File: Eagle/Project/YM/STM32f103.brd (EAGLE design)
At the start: 160 x 100 mm, 76 parts, among them IC1 YM3812, IC10 YM3812, IC11 YM3014B, IC12 LM358N, IC13 BA033CC0T, IC14 74ALS04N, IC15 6N136, IC2 YM3014B, IC3 LM358N, IC4 YM3812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

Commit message: LCD BOOTLOADER HEADER
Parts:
- added SV1: (no value), con-amp-mt:S06P
- added X3: (no value), con-weidmueller-sl35:90F-4
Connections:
- new net LCD-SPI-CS: SV1.4, U1.16
- net 3.3V: now also X3.1
- net 5V: now also SV1.5
- net EXP-SPI-CLK: now also SV1.1
- net EXP-SPI-MISO: now also SV1.2
- net EXP-SPI-MOSI: now also SV1.3
- net GND: now also SV1.6, X3.4
- net IO7: no longer U1.16
- net SW-CLK: now also X3.3
- net SW-DIO: now also X3.2
- net USART-TX-M4: now also X2.4
- net YM1-CS: no longer U1.51
- net YM2-CS: now also U1.51

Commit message: Eerste versie PCB - Nog niet gerout/gerouted/geroutedt. Ter review voor plaatsing componenten.
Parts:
- moved SL1 274.0 mm to (144.8, 68.6), turned to 270 degrees
- moved SL2 264.9 mm to (144.8, 36.8), turned to 270 degrees
- moved C38 259.5 mm to (144.8, 16.5)
- moved R6 256.8 mm to (148.6, 16.5)
- moved X3 251.1 mm to (63.5, 95.2), turned to 180 degrees
- moved CRYSTAL2 250.6 mm to (144.8, 20.3)
- moved C39 246.7 mm to (151.1, 2.54)
- moved R7 245.6 mm to (141.0, 16.5), turned to 180 degrees
- moved IC14 244.3 mm to (143.5, 8.89), turned to 180 degrees
- moved C30 244.2 mm to (132.1, 11.4)
- moved IC6 235.2 mm to (127.0, 66.0), turned to 180 degrees
- moved C29 230.6 mm to (120.7, 11.4)
- moved C28 229.1 mm to (120.7, 7.62)
- moved IC3 223.5 mm to (127.0, 90.2), turned to 180 degrees
- moved IC11 221.8 mm to (115.6, 17.8), turned to 180 degrees
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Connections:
- removed net N$28: C39.2
- net 5V: now also C39.2
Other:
- board size 160 x 100 mm -> 156.2 x 102.5 mm

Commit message: Eerste versie PCB
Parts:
- moved X2 66.1 mm to (26.7, 27.9), turned to 180 degrees
- moved J7 43.8 mm to (49.5, 17.8)
- moved J3 43.4 mm to (49.5, 6.35)
- moved SL2 43.2 mm to (144.8, 80.0)
- moved X3 24.7 mm to (39.4, 90.2)
- moved SV1 21.1 mm to (61.0, 11.4), turned to 90 degrees
- moved SL1 19.0 mm to (144.8, 49.5)
- moved J10 18.9 mm to (35.6, 17.8)
- moved J8 18.9 mm to (7.62, 17.8)
- moved J9 18.9 mm to (21.6, 17.8)
- moved J4 18.1 mm to (7.62, 6.35)
- moved J5 18.1 mm to (21.6, 6.35)
- moved J6 18.1 mm to (35.6, 6.35)
- moved C6 11.5 mm to (64.8, 66.0)
- moved C7 8.13 mm to (48.3, 74.9)
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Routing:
- net GND: track 0.00 -> 954.3 mm, vias 0 -> 45
- net 5V: track 0.00 -> 613.1 mm, vias 0 -> 24
- net 3.3V: track 0.00 -> 416.1 mm, vias 0 -> 3
- net YM-RST: track 0.00 -> 158.0 mm, vias 0 -> 2
- net YM-A0: track 0.00 -> 152.0 mm, vias 0 -> 2
- net YM-WR: track 0.00 -> 145.4 mm, vias 0 -> 2
- net USART-TX-M4: track 0.00 -> 144.5 mm, vias 0 -> 6
- net YM-D7: track 0.00 -> 135.6 mm, vias 0 -> 2
- net YM-D6: track 0.00 -> 129.6 mm, vias 0 -> 2
- net YM1-SYNC: track 0.00 -> 126.5 mm, vias 0 -> 4
- net YM-D5: track 0.00 -> 124.1 mm, vias 0 -> 2
- net YM-D4: track 0.00 -> 123.0 mm, vias 0 -> 2
- net YM-D1: track 0.00 -> 121.3 mm, vias 0 -> 2
- net YM-D0: track 0.00 -> 118.6 mm, vias 0 -> 4
- net YM-CLK-I: track 0.00 -> 112.3 mm
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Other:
- board size 156.2 x 102.5 mm -> 156.2 x 97.5 mm

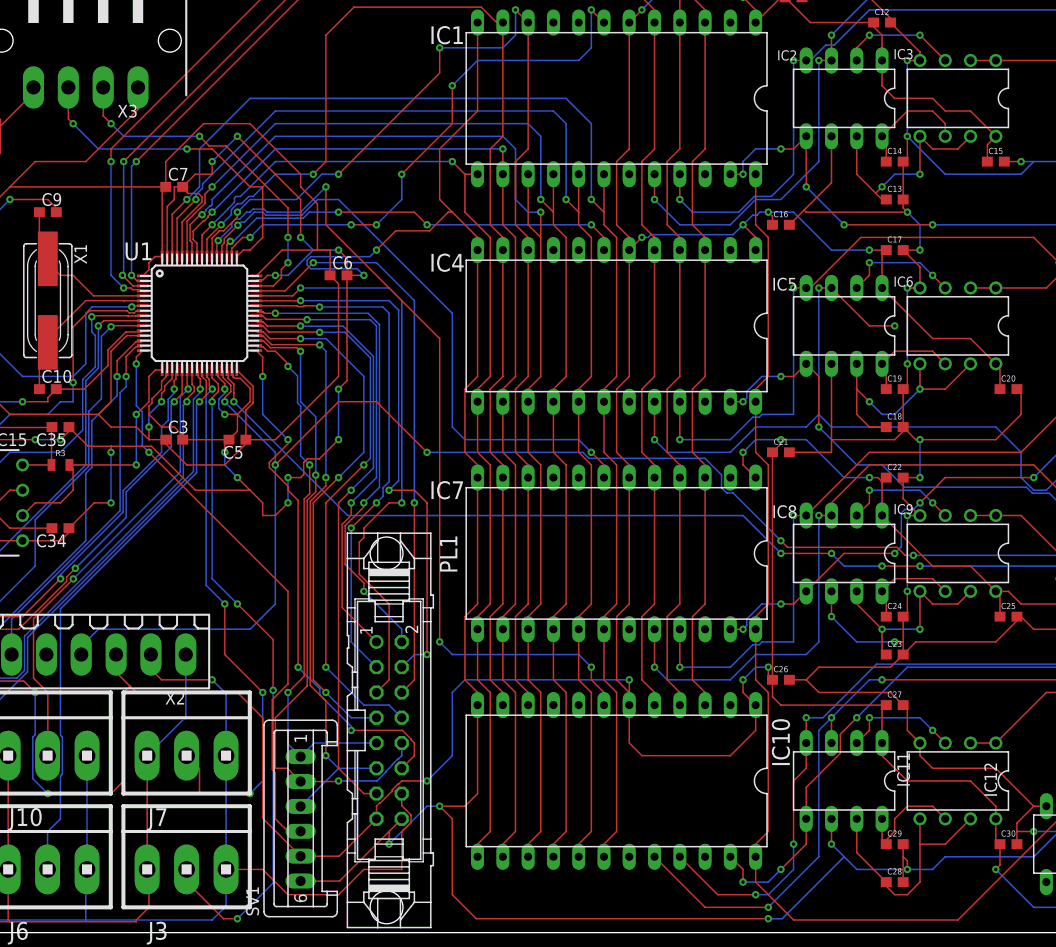
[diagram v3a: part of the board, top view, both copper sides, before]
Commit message: Opamp wire change
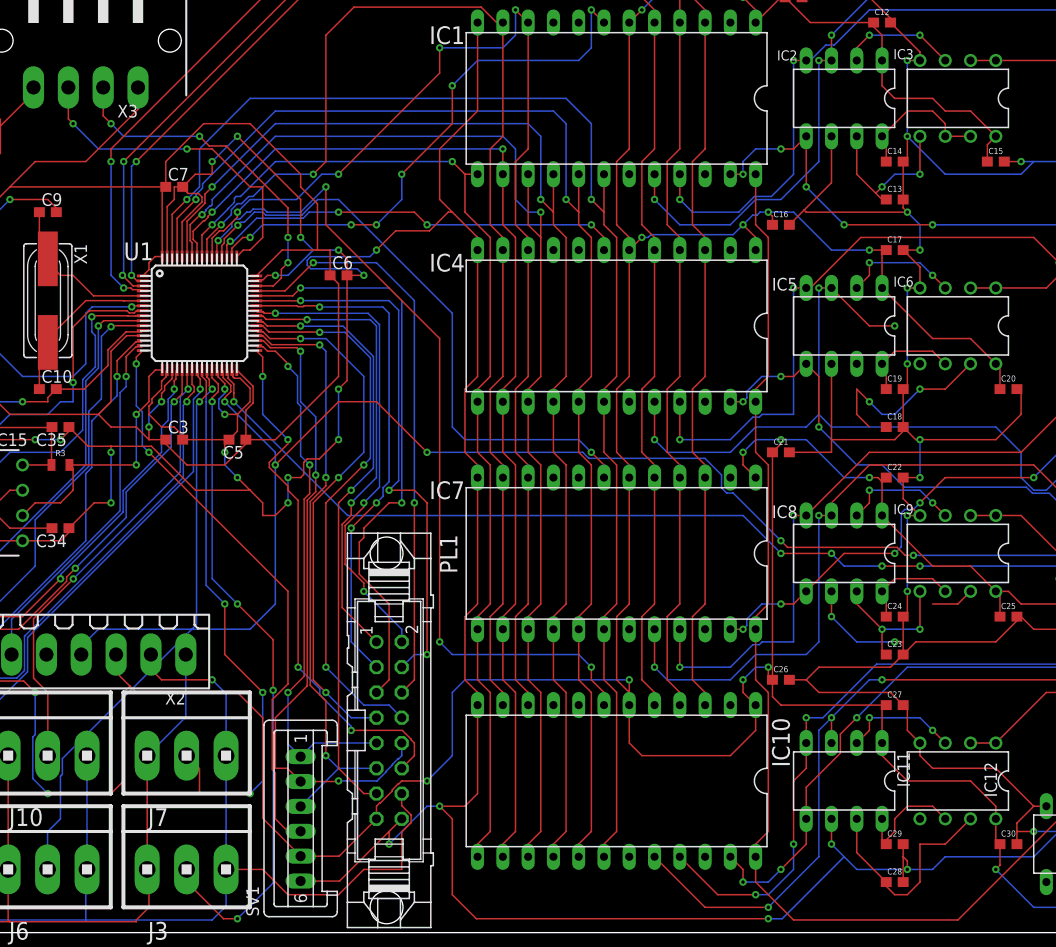
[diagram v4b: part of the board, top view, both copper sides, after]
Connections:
- removed net N$13: C29.1, IC11.MP, IC12.6
- new net N$15: C13.1, IC2.RB, IC3.5
- net N$10: now also C28.1, IC11.RB, IC12.5; no longer C24.1, IC8.MP, IC9.6
- net N$11: now also C24.1, IC8.MP, IC9.6; no longer C23.1, IC8.RB, IC9.5
- net N$14: now also C29.1, IC11.MP, IC12.6; no longer C28.1, IC11.RB, IC12.5
- net N$4: now also C18.1, IC5.RB, IC6.5; no longer C14.1, IC2.MP, IC3.6
- net N$5: now also C14.1, IC2.MP, IC3.6; no longer C13.1, IC2.RB, IC3.5
- net N$7: now also C23.1, IC8.RB, IC9.5; no longer C19.1, IC5.MP, IC6.6
- net N$8: now also C19.1, IC5.MP, IC6.6; no longer C18.1, IC5.RB, IC6.5
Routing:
- net N$15: track 0.00 -> 16.9 mm, vias 0 -> 2
- net N$4: track 11.9 -> 0.00 mm
- net N$13: track 11.7 -> 0.00 mm
- net N$5: track 23.0 -> 14.5 mm, vias 2 -> 0
- net N$11: track 21.3 -> 14.5 mm, vias 2 -> 0
- net N$7: track 10.1 -> 15.2 mm, vias 0 -> 2
- net N$8: track 25.7 -> 29.0 mm
- net N$10: track 10.1 -> 7.58 mm
- net N$14: track 24.7 -> 25.9 mm

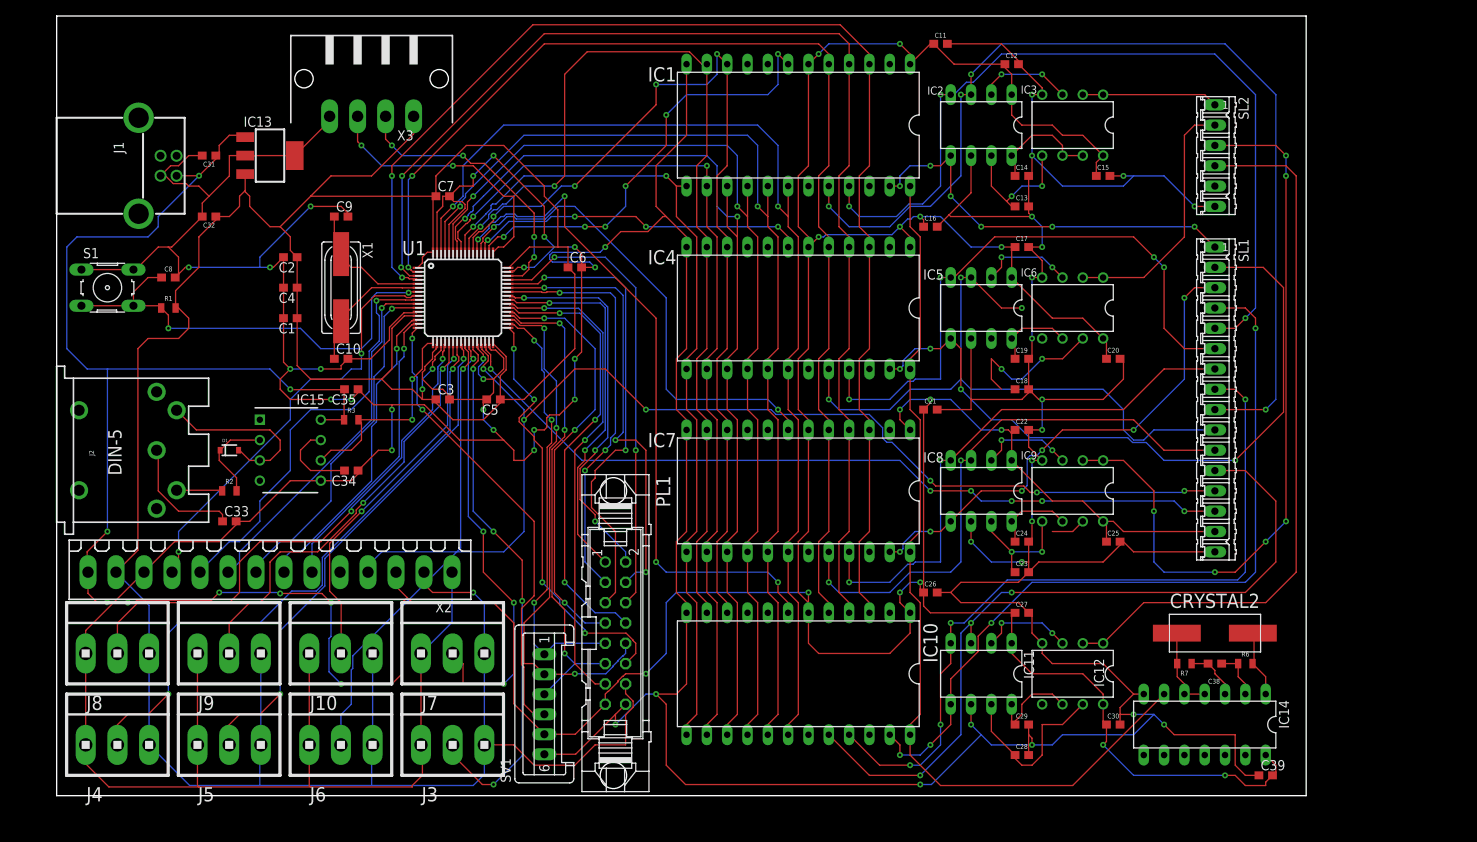
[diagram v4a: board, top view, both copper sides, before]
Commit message: v2.0 - voldoet aan de DRC van JLPCB - PCB staat klaar voor review project groep.
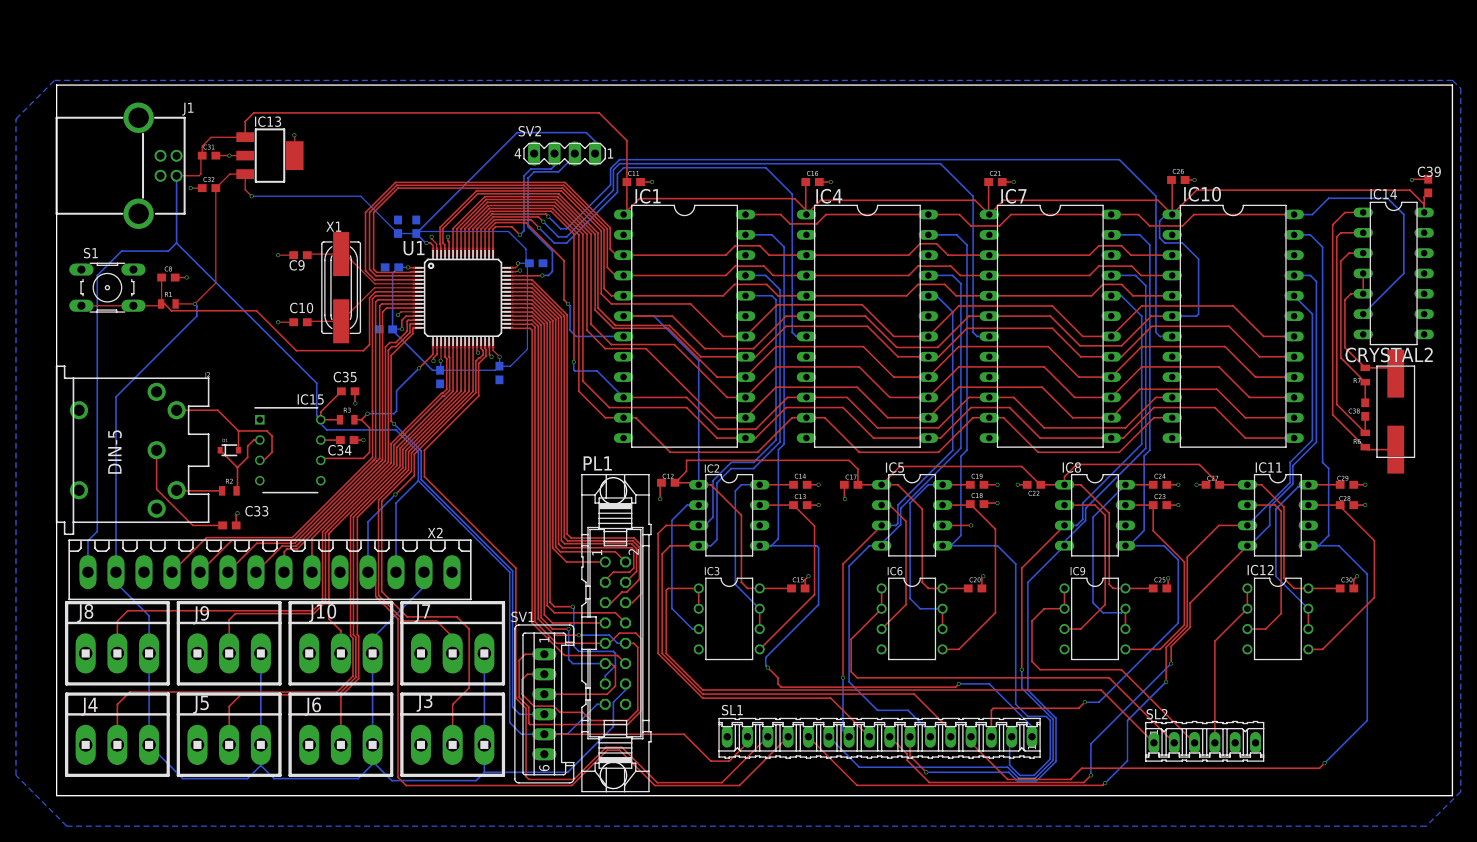
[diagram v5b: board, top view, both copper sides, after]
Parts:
- removed X3: (no value), con-weidmueller-sl35:90F-4
- added SV2: (no value), con-lstb:MA04-1
- moved C39 76.4 mm to (171.4, 76.2), turned to 270 degrees
- moved IC3 75.2 mm to (84.1, 22.1), turned to 270 degrees
- moved SL2 73.4 mm to (143.5, 6.60), turned to 0 degrees
- moved IC10 69.6 mm to (147.1, 58.7), turned to 270 degrees
- moved C12 67.7 mm to (76.5, 39.1), turned to 180 degrees
- moved C15 64.1 mm to (92.7, 25.9)
- moved IC14 61.1 mm to (167.1, 65.3), turned to 270 degrees
- moved C26 60.2 mm to (140.2, 77.0)
- moved SL1 59.4 mm to (102.9, 7.37), turned to 180 degrees
- moved IC2 58.1 mm to (84.1, 35.1), turned to 270 degrees
- moved C28 51.3 mm to (161.3, 36.3)
- moved C29 50.5 mm to (161.3, 38.9)
- moved C14 47.5 mm to (93.0, 38.9)
- moved C13 46.5 mm to (93.0, 36.3)
- moved IC6 43.7 mm to (106.9, 22.1), turned to 270 degrees
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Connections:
- net 3.3V: now also SV2.1; no longer X3.1
- net GND: now also SV2.4; no longer X3.4
- net SW-CLK: now also SV2.3; no longer X3.3
- net SW-DIO: now also SV2.2; no longer X3.2
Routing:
- net GND: track 954.3 -> 67.4 mm, vias 45 -> 38
- net 5V: track 613.1 -> 694.6 mm, vias 24 -> 0
- net 3.3V: track 416.1 -> 341.6 mm, vias 3 -> 8
- net DAC-OUT-3: track 90.6 -> 21.0 mm
- net DAC-OUT-0: track 17.0 -> 80.2 mm
- net DAC-OUT-2: track 94.2 -> 36.8 mm, vias 6 -> 0
- net YM1-CLK-O: track 51.9 -> 108.3 mm, vias 6 -> 2
- net EXP-SPI-CLK: track 53.9 -> 91.3 mm, vias 3 -> 0
- net YM1-SYNC: track 126.5 -> 89.5 mm, vias 4 -> 0
- net YM-D2: track 106.0 -> 140.0 mm, vias 2 -> 0
- net YM-RST: track 158.0 -> 125.1 mm, vias 2 -> 0
- net YM3-CS: track 60.9 -> 92.3 mm, vias 2 -> 1
- net N$27: track 8.54 -> 37.9 mm
- net YM4-CS: track 86.3 -> 115.2 mm, vias 4 -> 1
- net YM3-SYNC: track 71.3 -> 100.2 mm, vias 2 -> 1
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- added copper zone on layer 16, net GND
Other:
- board size 156.2 x 97.5 mm -> 174.5 x 88.8 mm

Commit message: v2.5 - IO expander update - moet nog steeds gepeerreviewd worden.
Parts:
- removed PL1: (no value), con-harting-v:16V
- added SV3: 2514-6002UB, 2514-6002UB:3M_2514-6002UB
- C10, C9: value (none) -> 20pF
- moved SL1 25.4 mm to (128.3, 7.37)
- moved SL2 14.5 mm to (158.0, 6.86)
- moved SV1 6.97 mm to (66.8, 7.62), flipped to the bottom, turned to 0 degrees
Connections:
- removed net EXP-SPI-A0: PL1.7, U1.37
- removed net EXP-SPI-A1: PL1.8, U1.38
- removed net EXP-SPI-NSS: PL1.12, U1.33
- removed net EXP3-INTA: PL1.5, U1.44
- removed net EXP3-INTB: PL1.6, U1.45
- new net EXP-SPI-NSS0: SV3.11, U1.37
- new net EXP-SPI-NSS1: SV3.10, U1.38
- new net OPEN: SV3.1
- net 3.3V: now also SV3.4; no longer PL1.14
- net 5V: now also SV3.3; no longer PL1.15
- net EXP-RST: now also SV3.9; no longer PL1.13
- net EXP-SPI-CLK: now also SV3.14; no longer PL1.9
- net EXP-SPI-MISO: now also SV3.13; no longer PL1.10
- net EXP-SPI-MOSI: now also SV3.12; no longer PL1.11
- net EXP1-INTA: now also SV3.8; no longer PL1.1
- net EXP1-INTB: now also SV3.7; no longer PL1.2
- net EXP2-INTA: now also SV3.5; no longer PL1.3
- net EXP2-INTB: now also SV3.6; no longer PL1.4
- net GND: now also SV3.2; no longer PL1.16
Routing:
- net EXP-SPI-NSS1: track 0.00 -> 98.0 mm
- net EXP-SPI-NSS0: track 0.00 -> 95.8 mm
- net 3.3V: track 341.6 -> 413.8 mm
- net EXP3-INTA: track 55.7 -> 0.00 mm
- net EXP3-INTB: track 55.0 -> 0.00 mm
- net EXP-SPI-NSS: track 53.4 -> 0.00 mm
- net EXP1-INTA: track 42.3 -> 94.8 mm
- net EXP-SPI-A1: track 51.6 -> 0.00 mm
- net EXP-SPI-A0: track 49.5 -> 0.00 mm
- net EXP1-INTB: track 45.1 -> 89.6 mm
- net YM3-SYNC: track 100.2 -> 65.1 mm
- net EXP-SPI-MOSI: track 66.8 -> 101.6 mm, vias 1 -> 0
- net EXP2-INTB: track 50.6 -> 84.8 mm
- net EXP-RST: track 59.1 -> 92.9 mm, vias 1 -> 0
- net EXP2-INTA: track 52.2 -> 84.6 mm
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
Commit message: v3.0 - PCB review aangepast
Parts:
- removed X2: (no value), con-weidmueller-sl35:180G-14
- added SV4: (no value), con-lsta:FE13
- moved C13 1.27 mm to (91.7, 36.3)
- moved C14 1.27 mm to (91.7, 38.9)
- moved C27 1.02 mm to (145.5, 38.9)
- moved C15 0.76 mm to (91.9, 25.9)
- moved C29 0.76 mm to (160.5, 38.9)
- moved C30 0.76 mm to (160.5, 25.9)
- moved C38 0.72 mm to (163.1, 48.8), turned to 0 degrees
- moved R6 0.72 mm to (163.1, 45.0), turned to 180 degrees
- moved R7 0.57 mm to (163.1, 52.8), turned to 0 degrees
- moved C23 0.51 mm to (137.4, 36.3)
- moved C24 0.51 mm to (137.4, 38.9)
- moved C22 0.51 mm to (122.7, 38.9)
- moved C28 0.51 mm to (160.8, 36.3)
- moved C39 0.25 mm to (171.7, 76.2), turned to 180 degrees
- moved C17 0.25 mm to (99.6, 38.9)
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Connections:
- removed net IO7: X2.5
- net 3.3V: now also SV4.12, SV4.2; no longer X2.13, X2.2
- net 5V: now also SV4.13, SV4.3; no longer X2.14, X2.3
- net GND: now also SV4.1, SV4.11; no longer X2.1, X2.12
- net IO1: now also SV4.10; no longer X2.11
- net IO2: now also SV4.9; no longer X2.10
- net IO3: now also SV4.8; no longer X2.9
- net IO4: now also SV4.7; no longer X2.8
- net IO5: now also SV4.6; no longer X2.7
- net IO6: now also SV4.5; no longer X2.6
- net USART-TX-M4: now also SV4.4; no longer X2.4
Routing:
- net USART-TX-M4: track 140.2 -> 159.1 mm
- net 5V: track 724.3 -> 733.6 mm
- net YM1-CLK-O: track 138.3 -> 129.1 mm
- net IO4: track 44.7 -> 53.2 mm
- net IO5: track 40.3 -> 48.3 mm
- net IO6: track 37.3 -> 45.2 mm
- net IO3: track 48.7 -> 56.3 mm
- net IO2: track 52.7 -> 59.3 mm
- net 3.3V: track 413.8 -> 420.1 mm
- net N$6: track 18.6 -> 24.5 mm
- net GND: track 66.1 -> 71.9 mm
- net IO1: track 56.6 -> 62.2 mm
- net N$3: track 19.6 -> 24.8 mm
- net N$8: track 27.5 -> 22.5 mm
- net N$11: track 27.2 -> 22.3 mm
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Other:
- board size 174.5 x 88.8 mm -> 174.2 x 88.8 mm
